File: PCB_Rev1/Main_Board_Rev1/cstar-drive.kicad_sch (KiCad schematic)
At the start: 15 parts, among them J10 B4B-PH-K-S, J9 B4B-PH-K-S, U2 L298N, X1 B2P-VH, X2 B2P-VH

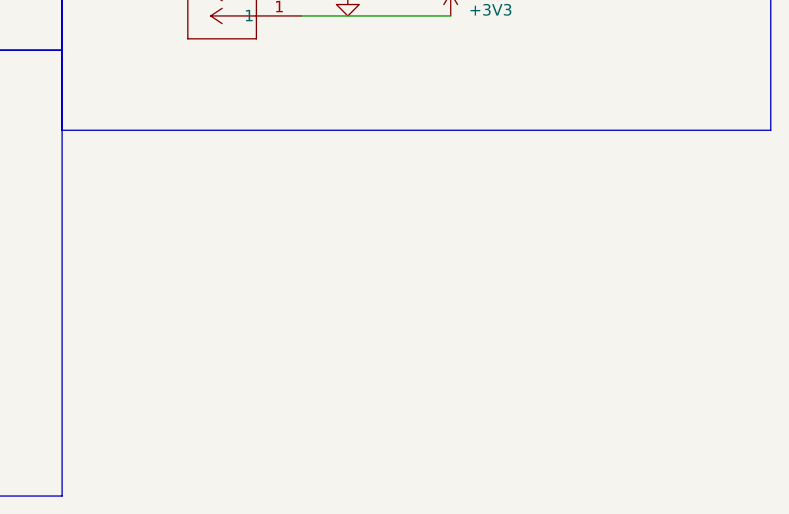
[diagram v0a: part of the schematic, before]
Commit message: Power nets updated in all schematics
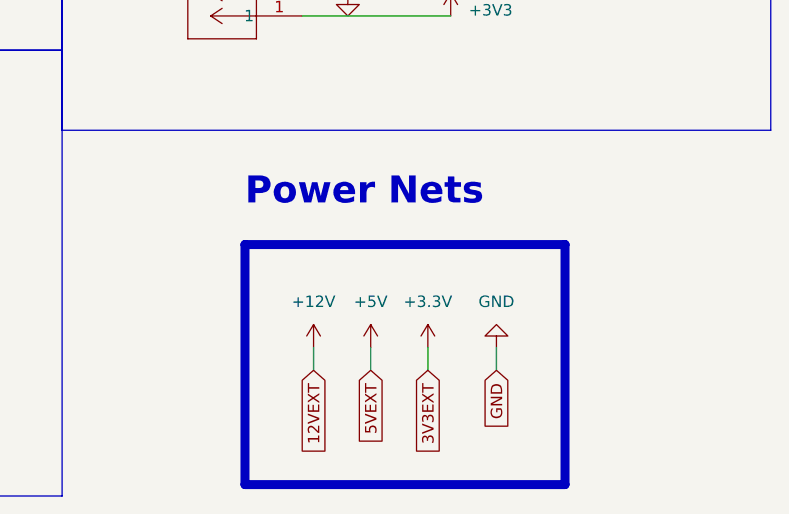
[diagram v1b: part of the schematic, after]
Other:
- note added: "Power Nets"

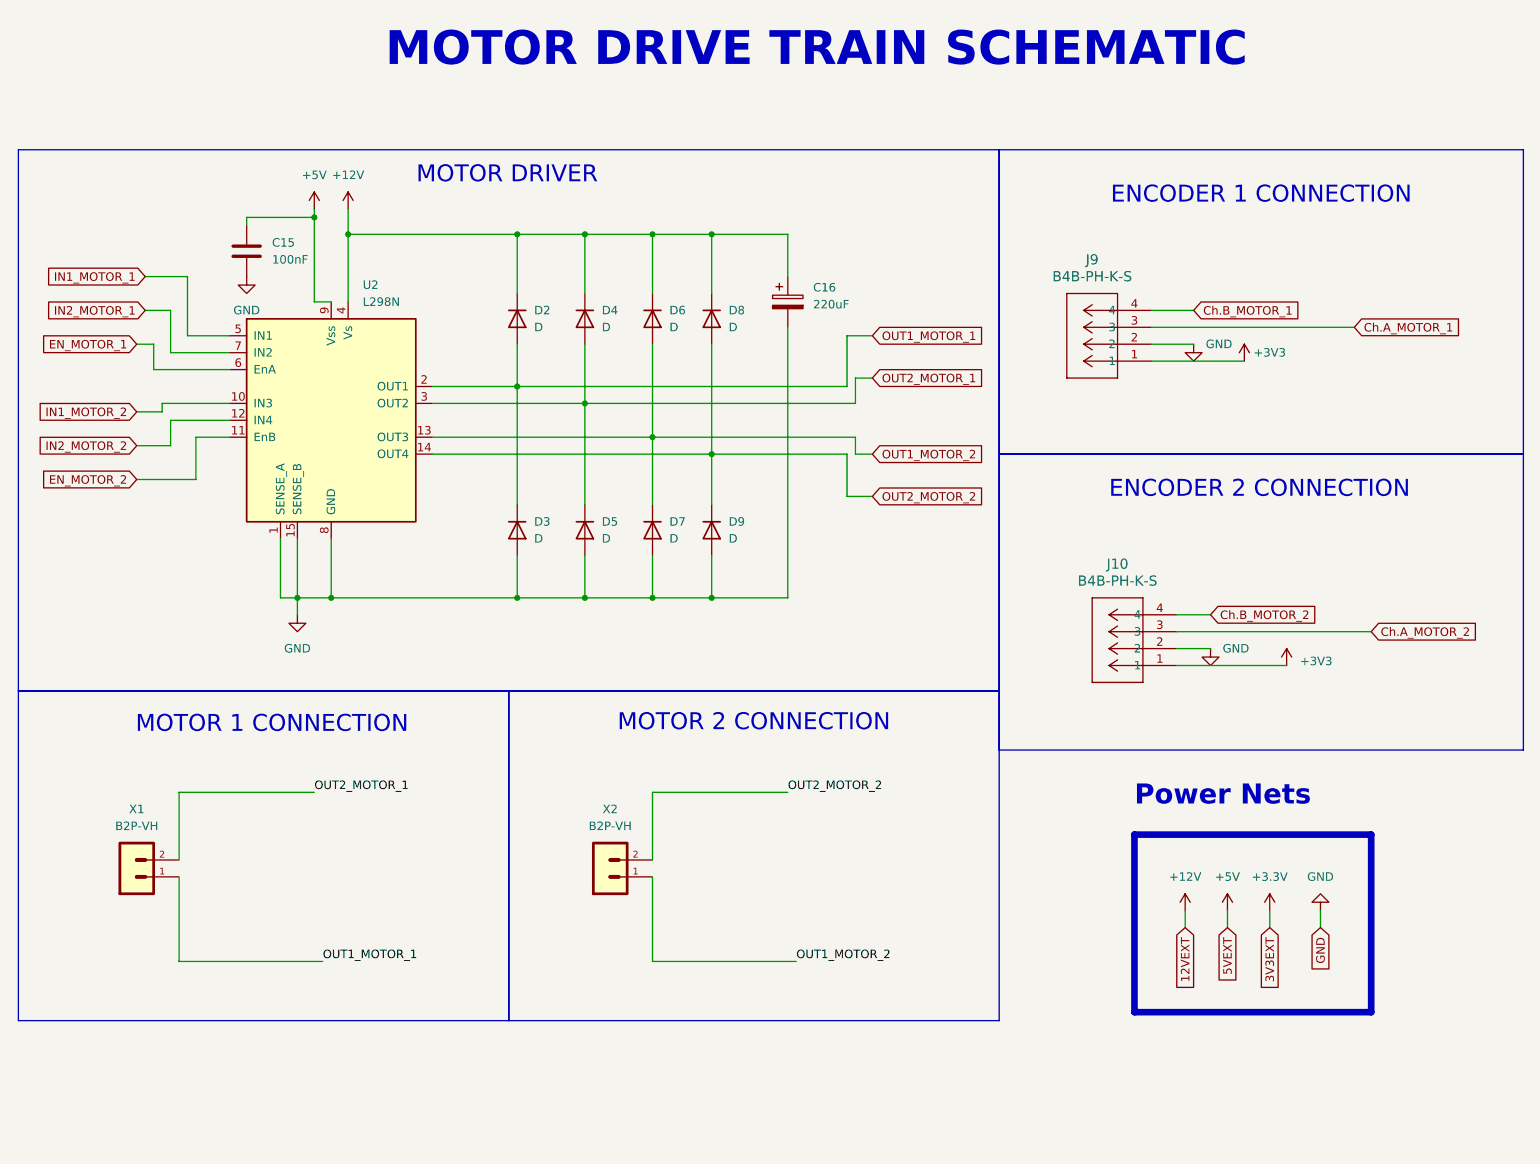
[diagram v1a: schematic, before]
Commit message: Connections to RPi GPIO Pins + Eliminating Errors from Layout
Global net connections made from RPi GPIO pins.
Error for mounting hole corrected -> mounting hole symbol imported into schematic and correct footprint assigned.
Warnings for J10, J11, J12 connectors resolved- imported footprint for the connector from online (error in the one imported from KiCAD libraries with pins S1 and S2 labeled as MP in the footprint)
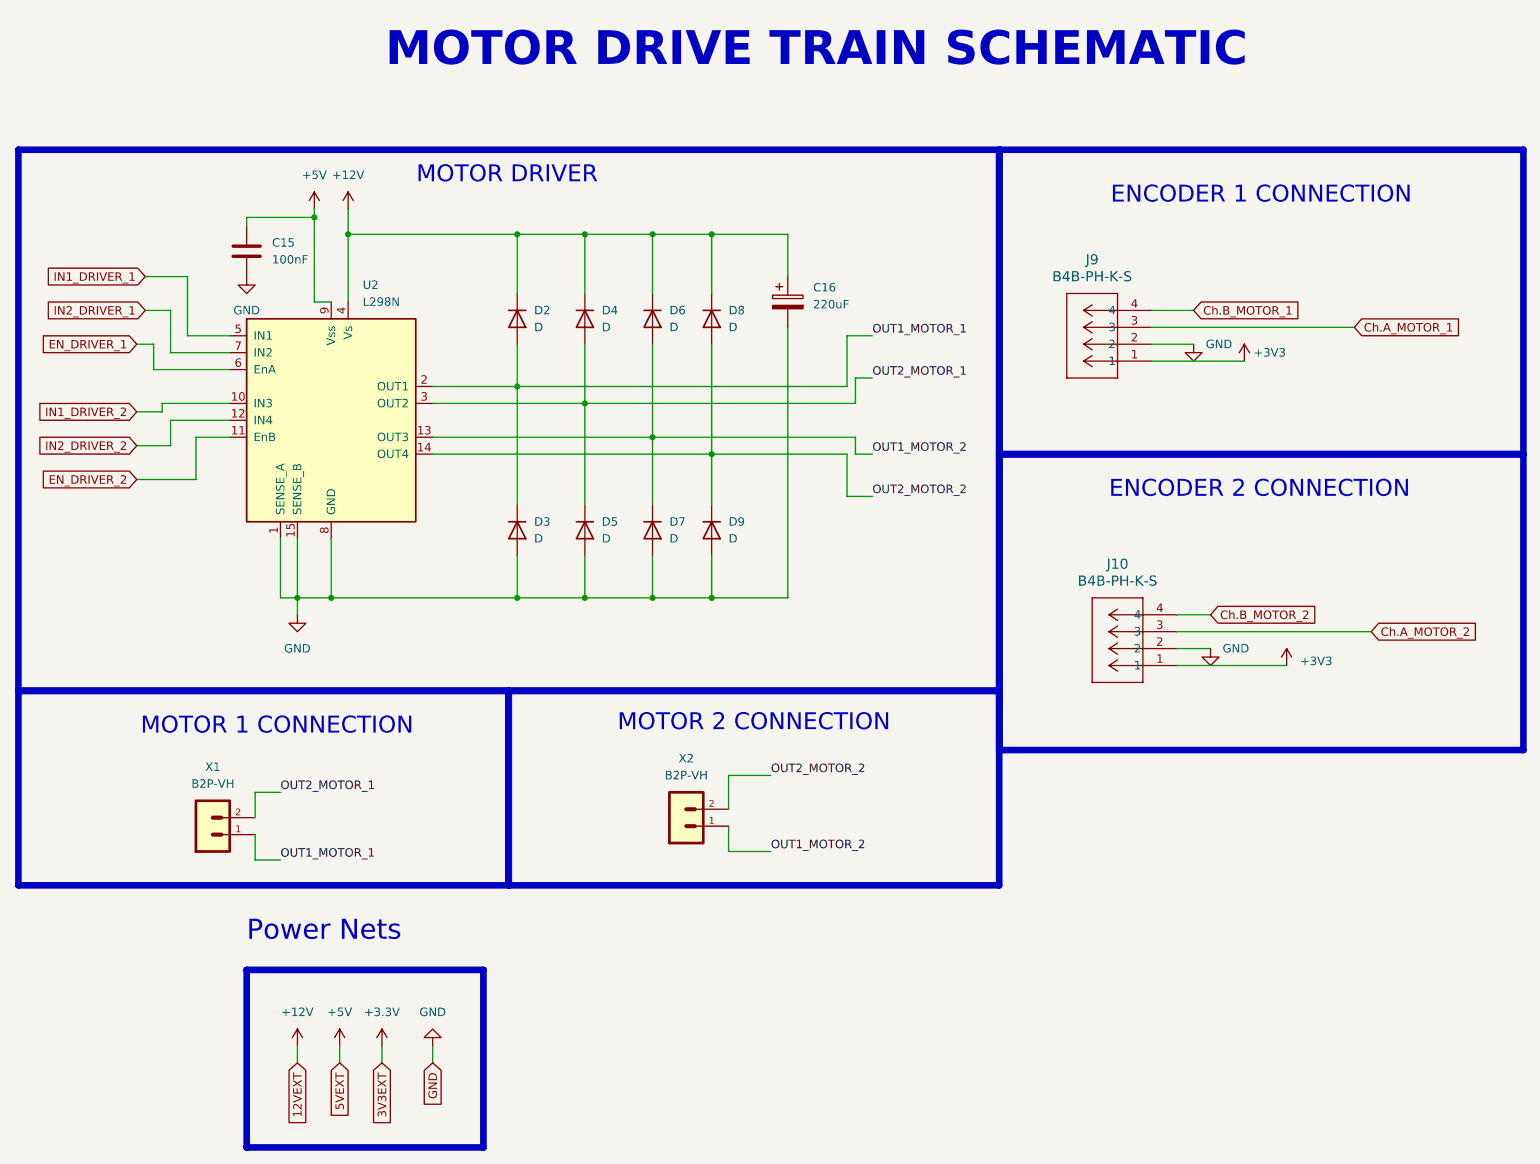
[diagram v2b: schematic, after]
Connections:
- net EN_MOTOR_1 renamed EN_DRIVER_1
- net EN_MOTOR_2 renamed EN_DRIVER_2
- net IN1_MOTOR_1 renamed IN1_DRIVER_1
- net IN1_MOTOR_2 renamed IN1_DRIVER_2
- net IN2_MOTOR_1 renamed IN2_DRIVER_1
- net IN2_MOTOR_2 renamed IN2_DRIVER_2
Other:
- moved on the sheet: X1, X2

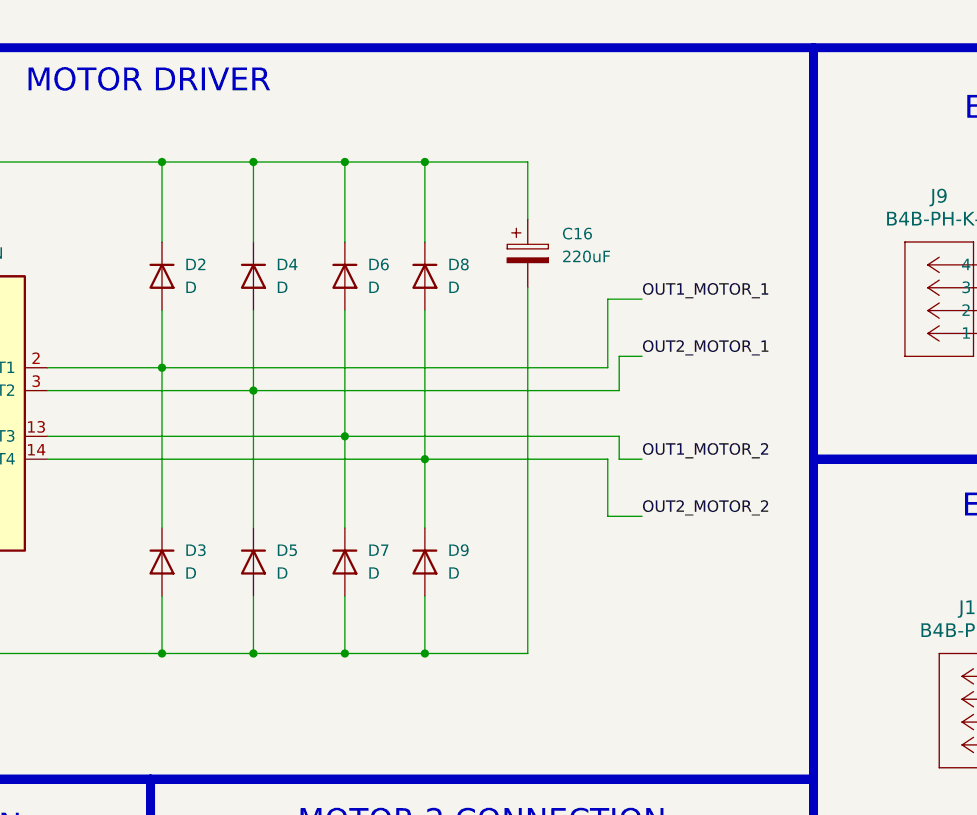
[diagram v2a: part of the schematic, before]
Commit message: TP for Motor Drive + U2 Routing
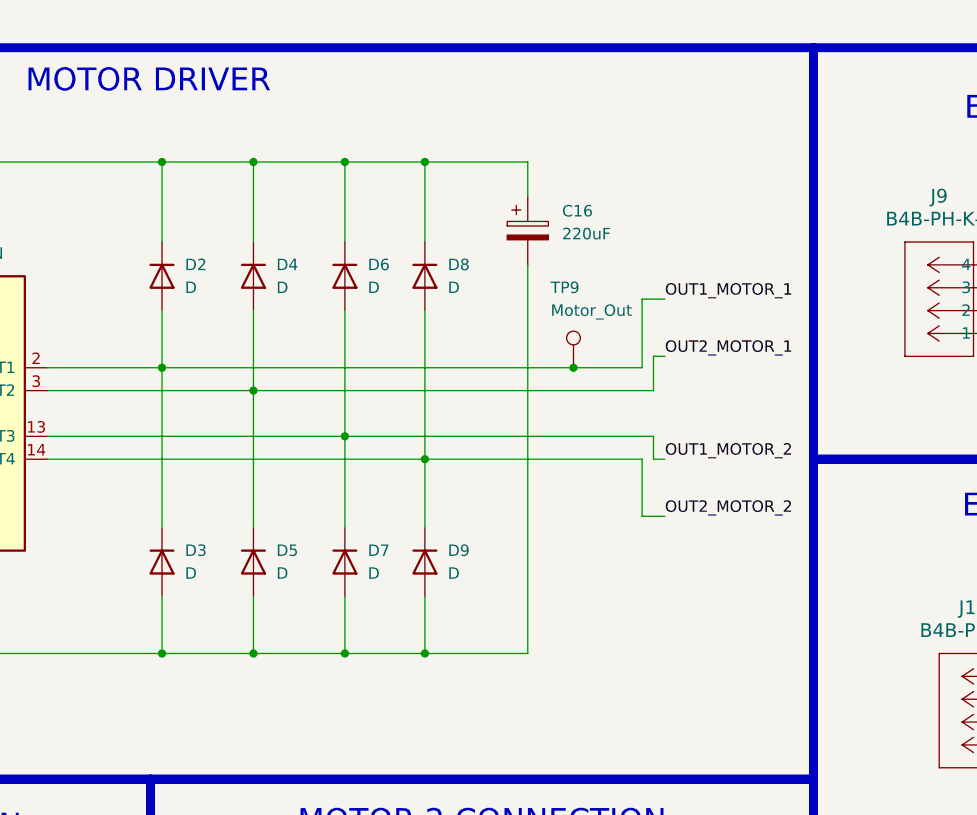
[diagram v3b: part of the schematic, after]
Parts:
- added TP9: Motor_Out, TestPoint:TestPoint_Pad_D2.0mm, symbol Connector:TestPoint
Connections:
- net OUT1_MOTOR_1: now also TP9.1
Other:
- moved on the sheet: C16
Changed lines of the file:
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@@
 	)
 	(junction
+		(at 146.05 78.74)
+		(diameter 0)
+		(color 0 0 0 0)
+	)
+	(junction
 		(at 129.54 55.88)
 		(diameter 0)
@@
 	(wire
 		(pts
-			(xy 110.49 81.28) (xy 151.13 81.28)
+			(xy 110.49 81.28) (xy 154.94 81.28)
 		)
 		(stroke
@@
 	(wire
 		(pts
-			(xy 151.13 88.9) (xy 153.67 88.9)
+			(xy 154.94 88.9) (xy 156.21 88.9)
 		)
 		(stroke
@@
 	(wire
 		(pts
-			(xy 149.86 78.74) (xy 149.86 71.12)
+			(xy 153.67 78.74) (xy 153.67 71.12)
 		)
 		(stroke
@@
 	(wire
 		(pts
-			(xy 120.65 86.36) (xy 151.13 86.36)
+			(xy 120.65 86.36) (xy 154.94 86.36)
 		)
 		(stroke
@@
 	(wire
 		(pts
-			(xy 151.13 77.47) (xy 153.67 77.47)
+			(xy 154.94 77.47) (xy 156.21 77.47)
 		)
 		(stroke
@@
 	(wire
 		(pts
-			(xy 151.13 81.28) (xy 151.13 77.47)
+			(xy 154.94 81.28) (xy 154.94 77.47)
 		)
 		(stroke
@@
 	(wire
 		(pts
-			(xy 151.13 86.36) (xy 151.13 88.9)
+			(xy 154.94 86.36) (xy 154.94 88.9)
 		)
 		(stroke
@@
 	(wire
 		(pts
-			(xy 149.86 71.12) (xy 153.67 71.12)
+			(xy 153.67 71.12) (xy 156.21 71.12)
 		)
 		(stroke
@@
 	(wire
 		(pts
-			(xy 100.33 78.74) (xy 149.86 78.74)
+			(xy 100.33 78.74) (xy 146.05 78.74)
 		)
 		(stroke
@@
 	(wire
 		(pts
-			(xy 149.86 95.25) (xy 153.67 95.25)
+			(xy 153.67 95.25) (xy 156.21 95.25)
 		)
 		(stroke
@@
 	(wire
 		(pts
-			(xy 129.54 88.9) (xy 149.86 88.9)
+			(xy 129.54 88.9) (xy 153.67 88.9)
 		)
 		(stroke
@@
 	(wire
 		(pts
-			(xy 149.86 88.9) (xy 149.86 95.25)
+			(xy 153.67 88.9) (xy 153.67 95.25)
 		)
 		(stroke
@@
 	(wire
 		(pts
-			(xy 140.97 69.85) (xy 140.97 110.49)
+			(xy 140.97 67.31) (xy 140.97 110.49)
 		)
 		(stroke
@@
 	(wire
 		(pts
+			(xy 146.05 78.74) (xy 153.67 78.74)
+		)
+		(stroke
+			(width 0)
+			(type default)
+		)
+	)
+	(wire
+		(pts
 			(xy 129.54 55.88) (xy 140.97 55.88)
 		)
@@
 	(wire
 		(pts
-			(xy 140.97 55.88) (xy 140.97 62.23)
+			(xy 140.97 55.88) (xy 140.97 59.69)
 		)
 		(stroke
@@
 	)
 	(label "OUT2_MOTOR_2"
-		(at 153.67 95.25 0)
+		(at 156.21 95.25 0)
 		(fields_autoplaced yes)
 		(effects
@@
 	)
 	(label "OUT2_MOTOR_1"
-		(at 153.67 77.47 0)
+		(at 156.21 77.47 0)
 		(fields_autoplaced yes)
 		(effects
@@
 	)
 	(label "OUT1_MOTOR_1"
-		(at 153.67 71.12 0)
+		(at 156.21 71.12 0)
 		(fields_autoplaced yes)
 		(effects
@@
 	)
 	(label "OUT1_MOTOR_2"
-		(at 153.67 88.9 0)
+		(at 156.21 88.9 0)
 		(fields_autoplaced yes)
 		(effects
@@
 	)
 	(symbol
+		(lib_id "Connector:TestPoint")
+		(at 146.05 78.74 0)
+		(unit 1)
+		(exclude_from_sim no)
+		(in_bom yes)
+		(on_board yes)
+		(dnp no)
+		(property "Reference" "TP9"
+			(at 143.51 69.85 0)
+			(effects
+				(font
+					(size 1.27 1.27)
+				)
+				(justify left)
+			)
+		)
+		(property "Value" "Motor_Out"
+			(at 143.51 72.39 0)
+			(effects
+				(font
+					(size 1.27 1.27)
+				)
+				(justify left)
+			)
+		)
+		(property "Footprint" "TestPoint:TestPoint_Pad_D2.0mm"
+			(at 151.13 78.74 0)
+			(effects
+				(font
+					(size 1.27 1.27)
+				)
+				(hide yes)
+			)
+		)
+		(property "Datasheet" "~"
+			(at 151.13 78.74 0)
+			(effects
+				(font
+					(size 1.27 1.27)
+				)
+				(hide yes)
+			)
+		)
+		(property "Description" ""
+			(at 146.05 78.74 0)
+			(effects
+				(font
+					(size 1.27 1.27)
+				)
+				(hide yes)
+			)
+		)
+		(pin "1"
+		)
+		(instances
+			(project "Main_Board_Rev1"
+				(path "/8f5a23de-a1fa-4202-92fb-c2ac3de0338c/0ea4e72d-54a3-4446-a173-a8fc45c421fe"
+					(reference "TP9")
+					(unit 1)
+				)
+			)
+		)
+	)
+	(symbol
 		(lib_id "Device:D")
 		(at 129.54 100.33 270)
@@
 	(symbol
 		(lib_id "Device:C_Polarized")
-		(at 140.97 66.04 0)
+		(at 140.97 63.5 0)
 		(unit 1)
 		(exclude_from_sim no)
@@
 		(fields_autoplaced yes)
 		(property "Reference" "C16"
-			(at 144.78 63.8809 0)
+			(at 144.78 61.3409 0)
 			(effects
 				(font
@@
 		)
 		(property "Value" "220uF"
-			(at 144.78 66.4209 0)
+			(at 144.78 63.8809 0)
 			(effects
 				(font
@@
 		)
 		(property "Footprint" "Footprints:Cap_Polarized_220uF"
-			(at 141.9352 69.85 0)
+			(at 141.9352 67.31 0)
 			(effects
 				(font
@@
 		)
 		(property "Datasheet" "~"
-			(at 140.97 66.04 0)
+			(at 140.97 63.5 0)
 			(effects
 				(font
@@
 		)
 		(property "Description" "Polarized capacitor"
-			(at 140.97 66.04 0)
+			(at 140.97 63.5 0)
 			(effects
 				(font
